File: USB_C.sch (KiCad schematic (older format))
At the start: 4 parts, among them J1 USB_C_Receptacle

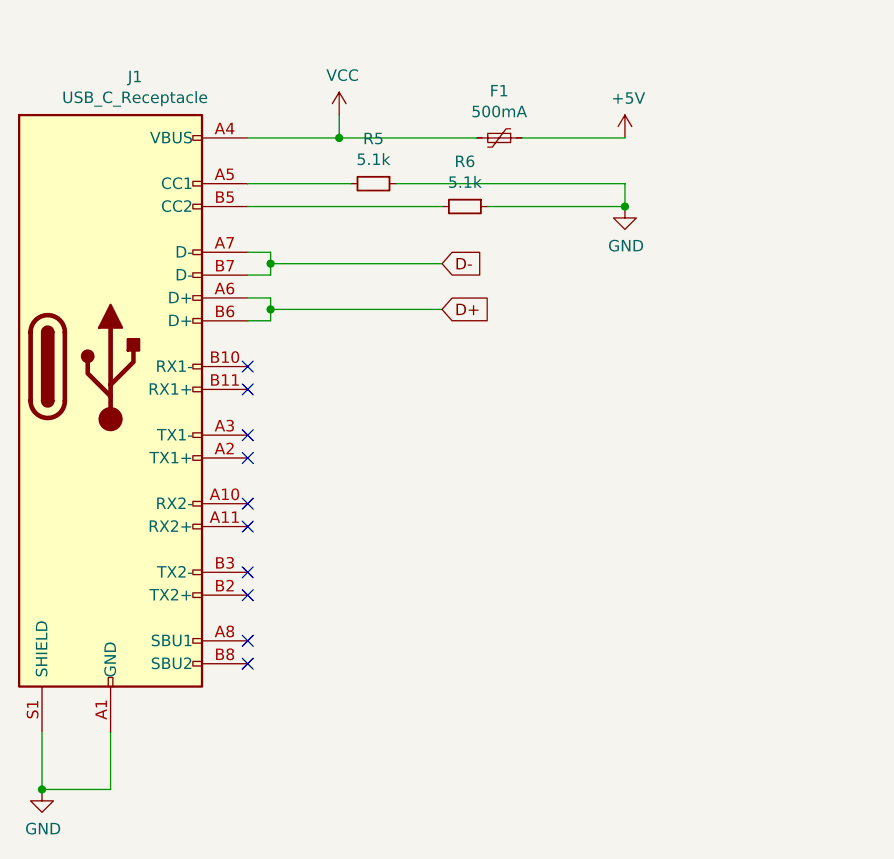
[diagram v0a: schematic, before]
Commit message: Assigned footprint
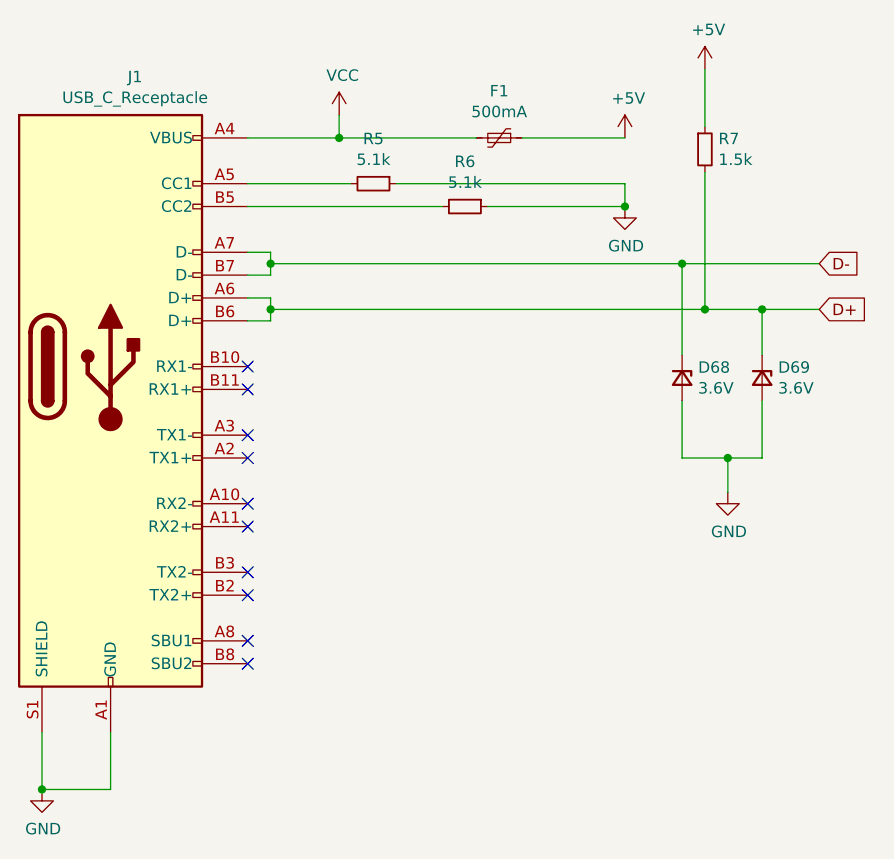
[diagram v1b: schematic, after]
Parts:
- added D68, D69: 3.6V, Diode_SMD:D_0805_2012Metric, symbol Device:D_Zener_Small
- added R7: 1.5k, Resistor_SMD:R_0805_2012Metric, symbol Device:R_Small
- F1: footprint (none) -> Fuse:Fuse_1206_3216Metric
- J1: footprint (none) -> Connector_USB:USB_C_Receptacle_GCT_USB4085
- R5, R6: footprint (none) -> Resistor_SMD:R_0805_2012Metric
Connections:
- net +5V: now also R7.1
- net D+: now also D69.1 (K), R7.2
- net D-: now also D68.1 (K)
- net GND: now also D68.2 (A), D69.2 (A)
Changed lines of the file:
@@
 F 0 "J1" H 4007 4567 50  0000 C CNN
 F 1 "USB_C_Receptacle" H 4007 4476 50  0000 C CNN
-F 2 "" H 4050 3300 50  0001 C CNN
+F 2 "Connector_USB:USB_C_Receptacle_GCT_USB4085" H 4050 3300 50  0001 C CNN
 F 3 "https://www.usb.org/sites/default/files/documents/usb_type-c.zip" H 4050 3300 50  0001 C CNN
 	1    3900 3300
@@
 F 0 "R5" V 4854 2500 50  0000 C CNN
 F 1 "5.1k" V 4945 2500 50  0000 C CNN
-F 2 "" H 5050 2500 50  0001 C CNN
+F 2 "Resistor_SMD:R_0805_2012Metric" H 5050 2500 50  0001 C CNN
 F 3 "~" H 5050 2500 50  0001 C CNN
 	1    5050 2500
@@
 F 0 "R6" V 5254 2600 50  0000 C CNN
 F 1 "5.1k" V 5345 2600 50  0000 C CNN
-F 2 "" H 5450 2600 50  0001 C CNN
+F 2 "Resistor_SMD:R_0805_2012Metric" H 5450 2600 50  0001 C CNN
 F 3 "~" H 5450 2600 50  0001 C CNN
 	1    5450 2600
@@
 F 0 "F1" V 5395 2300 50  0000 C CNN
 F 1 "500mA" V 5486 2300 50  0000 C CNN
-F 2 "" H 5650 2100 50  0001 L CNN
+F 2 "Fuse:Fuse_1206_3216Metric" H 5650 2100 50  0001 L CNN
 F 3 "~" H 5600 2300 50  0001 C CNN
 	1    5600 2300
@@
 Wire Wire Line
 	4600 3100 4500 3100
-Text GLabel 5350 2850 2    50   Input ~ 0
+Text GLabel 7000 2850 2    50   Input ~ 0
 D-
-Text GLabel 5350 3050 2    50   Input ~ 0
+Text GLabel 7000 3050 2    50   Input ~ 0
 D+
-Wire Wire Line
-	4600 3050 5350 3050
 Connection ~ 4600 3050
 Wire Wire Line
 	4600 3050 4600 3100
-Wire Wire Line
-	5350 2850 4600 2850
 Connection ~ 4600 2850
 Wire Wire Line
 	4600 2850 4600 2900
+$Comp
+L Device:R_Small R7
+U 1 1 5F1E95BA
+P 6500 2350
+F 0 "R7" H 6559 2396 50  0000 L CNN
+F 1 "1.5k" H 6559 2305 50  0000 L CNN
+F 2 "Resistor_SMD:R_0805_2012Metric" H 6500 2350 50  0001 C CNN
+F 3 "~" H 6500 2350 50  0001 C CNN
+	1    6500 2350
+	1    0    0    -1
+$EndComp
+Wire Wire Line
+	4600 2850 6400 2850
+Wire Wire Line
+	4600 3050 6500 3050
+$Comp
+L power:+5V #PWR0117
+U 1 1 5F1EB50A
+P 6500 2000
+F 0 "#PWR0117" H 6500 1850 50  0001 C CNN
+F 1 "+5V" H 6515 2173 50  0000 C CNN
+F 2 "" H 6500 2000 50  0001 C CNN
+F 3 "" H 6500 2000 50  0001 C CNN
+	1    6500 2000
+	1    0    0    -1
+$EndComp
+Wire Wire Line
+	6500 2000 6500 2250
+$Comp
+L Device:D_Zener_Small D68
+U 1 1 5F23B53F
+P 6400 3350
+F 0 "D68" V 6354 3420 50  0000 L CNN
+F 1 "3.6V" V 6445 3420 50  0000 L CNN
+F 2 "Diode_SMD:D_0805_2012Metric" V 6400 3350 50  0001 C CNN
+F 3 "~" V 6400 3350 50  0001 C CNN
+	1    6400 3350
+	0    1    1    0
+$EndComp
+$Comp
+L Device:D_Zener_Small D69
+U 1 1 5F23BD54
+P 6750 3350
+F 0 "D69" V 6704 3420 50  0000 L CNN
+F 1 "3.6V" V 6795 3420 50  0000 L CNN
+F 2 "Diode_SMD:D_0805_2012Metric" V 6750 3350 50  0001 C CNN
+F 3 "~" V 6750 3350 50  0001 C CNN
+	1    6750 3350
+	0    1    1    0
+$EndComp
+$Comp
+L power:GND #PWR0118
+U 1 1 5F23CF84
+P 6600 3850
+F 0 "#PWR0118" H 6600 3600 50  0001 C CNN
+F 1 "GND" H 6605 3677 50  0000 C CNN
+F 2 "" H 6600 3850 50  0001 C CNN
+F 3 "" H 6600 3850 50  0001 C CNN
+	1    6600 3850
+	1    0    0    -1
+$EndComp
+Wire Wire Line
+	6400 3250 6400 2850
+Connection ~ 6400 2850
+Wire Wire Line
+	6750 3250 6750 3050
+Connection ~ 6750 3050
+Wire Wire Line
+	6750 3050 7000 3050
+Wire Wire Line
+	6400 3450 6400 3700
+Wire Wire Line
+	6400 3700 6600 3700
+Wire Wire Line
+	6750 3700 6750 3450
+Wire Wire Line
+	6600 3850 6600 3700
+Connection ~ 6600 3700
+Wire Wire Line
+	6600 3700 6750 3700
+Wire Wire Line
+	6400 2850 7000 2850
+Wire Wire Line
+	6500 2450 6500 3050
+Connection ~ 6500 3050
+Wire Wire Line
+	6500 3050 6750 3050
 $EndSCHEMATC
